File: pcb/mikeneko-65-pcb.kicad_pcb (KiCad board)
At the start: 2 copper layers, 303.8 x 94.2 mm, 161 parts, among them J1 JST SH 4-pin, J2 AVR-ISP-6, SW1 Reset, U1 SRV05-4, U2 ATmega32U4-AU, Y1 16MHz

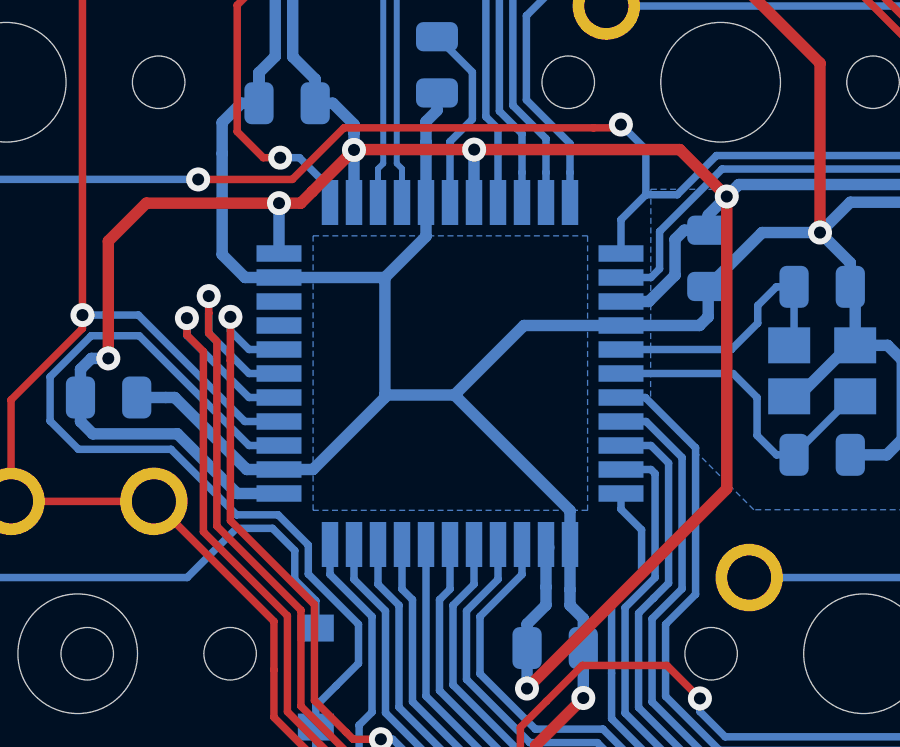
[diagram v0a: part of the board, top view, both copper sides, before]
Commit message: 回路図から基板を更新。
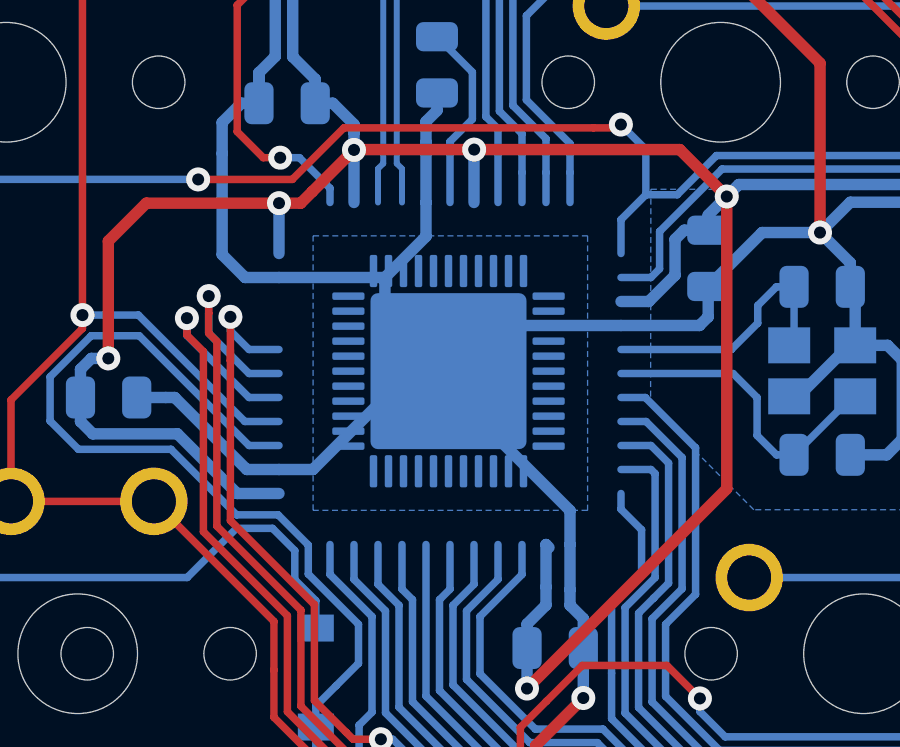
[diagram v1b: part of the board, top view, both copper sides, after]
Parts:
- U2: value ATmega32U4-AU -> ATmega32U4-MU; footprint Package_QFP:TQFP-44_10x10mm_P0.8mm -> Package_DFN_QFN:QFN-44-1EP_7x7mm_P0.5mm_EP5.2x5.2mm
- moved U2 0.09 mm to (28.5, 37.7)

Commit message: atmega32u4-muの配線を修正。 配線の太さの定義を追加、配線間隔の最小値を0.127mmに変更
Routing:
- net +5V: track 123.2 -> 139.1 mm
- net ROW2: track 301.5 -> 304.3 mm
- net /MCU_D-: track 19.2 -> 21.9 mm
- net XTAL1: track 10.5 -> 13.2 mm
- net ROW1: track 284.9 -> 287.5 mm
- net COL0: track 99.8 -> 102.4 mm
- net COL6: track 212.1 -> 214.6 mm
- net COL1: track 113.8 -> 116.3 mm
- net /MCU_D+: track 18.4 -> 20.9 mm
- net ROW0: track 295.7 -> 298.2 mm
- net XTAL2: track 9.00 -> 11.5 mm
- net ROW4: track 346.6 -> 349.1 mm
- net Net-(C7-Pad1): track 6.32 -> 8.63 mm
- net SCK: track 45.7 -> 48.0 mm
- net ROW3: track 300.9 -> 303.1 mm
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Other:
- net class D: clearance 0.2 -> 0.127
- net class Default: clearance 0.2 -> 0.127
- net class Power: clearance 0.2 -> 0.127
- rule trace_clearance: 0.2 -> 0.127
